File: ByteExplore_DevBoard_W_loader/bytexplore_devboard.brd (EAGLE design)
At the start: 68.6 x 53.3 mm, 87 parts, among them IC1 LM1117MPX-3.3, IC2 STM32F107RCT, IC4 MIC5219, IC6 STM32F103C8T, IC8 CP2101, J1 POWER_JACKPTH, Y1 SMD-CRYSTAL-8MHZ-20PF-20PPM(2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

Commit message: initial commit
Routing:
- net VDDA_PIN: track 47.5 -> 52.8 mm
- net GND: track 133.6 -> 137.7 mm, vias 53 -> 58
- added copper zone on layer 1, net N$49

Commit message: initial commit
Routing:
- net T_JTCK: track 58.0 -> 58.5 mm
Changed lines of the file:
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@@
 <drawing>
 <settings>
-<setting alwaysvectorfont="yes"/>
+<setting alwaysvectorfont="no"/>
 <setting verticaltext="up"/>
 </settings>
@@
 <wire x1="18.51" y1="22.86" x2="18.51" y2="22.98" width="0.25" layer="1"/>
 <via x="18.51" y="22.98" extent="1-16" drill="0.55"/>
-<wire x1="21.99" y1="24.57" x2="20.4" y2="22.98" width="0.25" layer="16"/>
-<wire x1="20.4" y1="22.98" x2="18.51" y2="22.98" width="0.25" layer="16"/>
-<wire x1="21.99" y1="24.57" x2="21.99" y2="26.55" width="0.25" layer="16"/>
-<wire x1="20.52" y1="28.02" x2="21.99" y2="26.55" width="0.254" layer="16"/>
+<wire x1="21.99" y1="23.7" x2="21.27" y2="22.98" width="0.25" layer="16"/>
+<wire x1="21.27" y1="22.98" x2="18.51" y2="22.98" width="0.25" layer="16"/>
+<wire x1="21.99" y1="23.7" x2="21.99" y2="27.15" width="0.25" layer="16"/>
+<wire x1="20.52" y1="28.62" x2="21.99" y2="27.15" width="0.254" layer="16"/>
 <via x="20.82" y="39.15" extent="1-16" drill="0.55"/>
 <wire x1="24.98" y1="39.53" x2="24.15" y2="38.7" width="0.254" layer="1"/>
@@
 <wire x1="25.44" y1="33.93" x2="22.32" y2="30.81" width="0.254" layer="16"/>
 <wire x1="21.33" y1="30.81" x2="20.52" y2="30" width="0.254" layer="16"/>
-<wire x1="20.52" y1="30" x2="20.52" y2="28.02" width="0.254" layer="16"/>
+<wire x1="20.52" y1="30" x2="20.52" y2="28.62" width="0.254" layer="16"/>
 <wire x1="11.955" y1="45.615" x2="11.955" y2="41.475" width="0.254" layer="16"/>
 <wire x1="11.955" y1="41.475" x2="13.5755375" y2="39.8544625" width="0.254" layer="16"/>

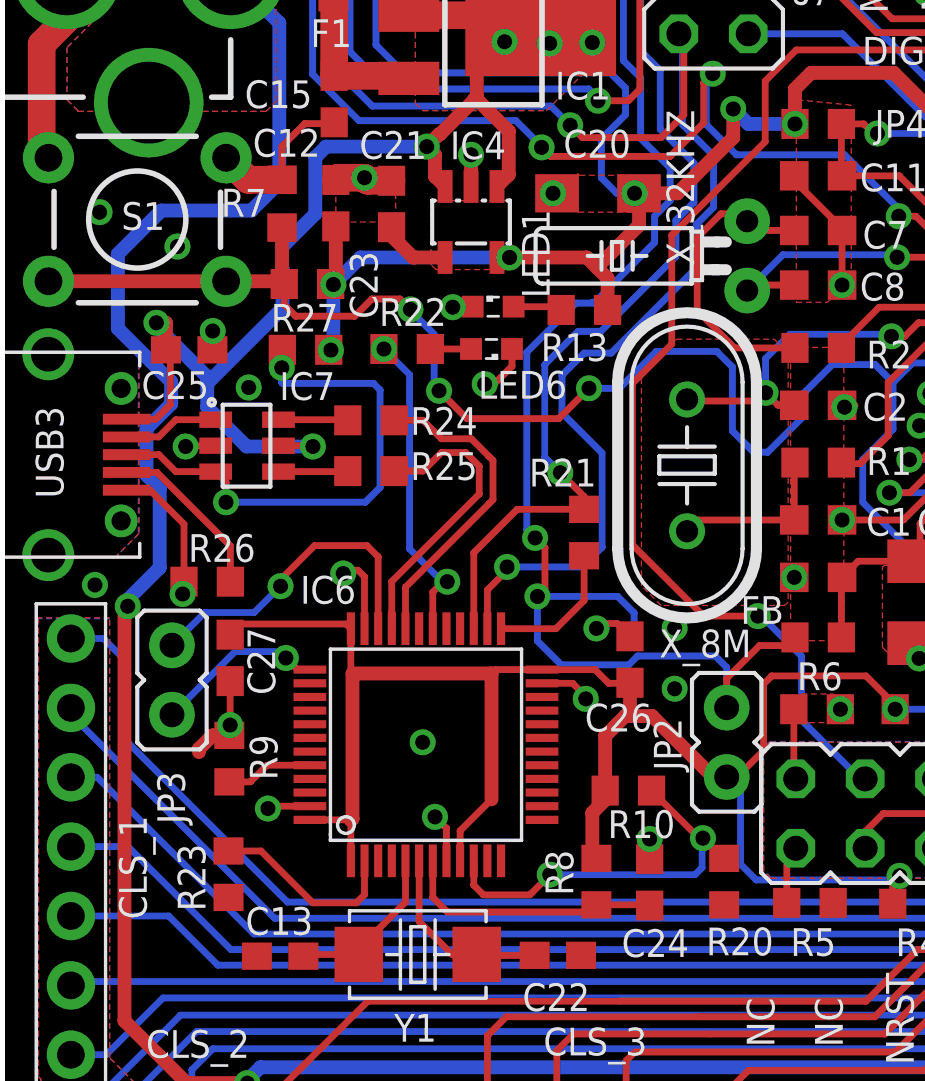
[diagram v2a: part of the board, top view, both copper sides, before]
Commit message: initial commit
change in power 3V wiring
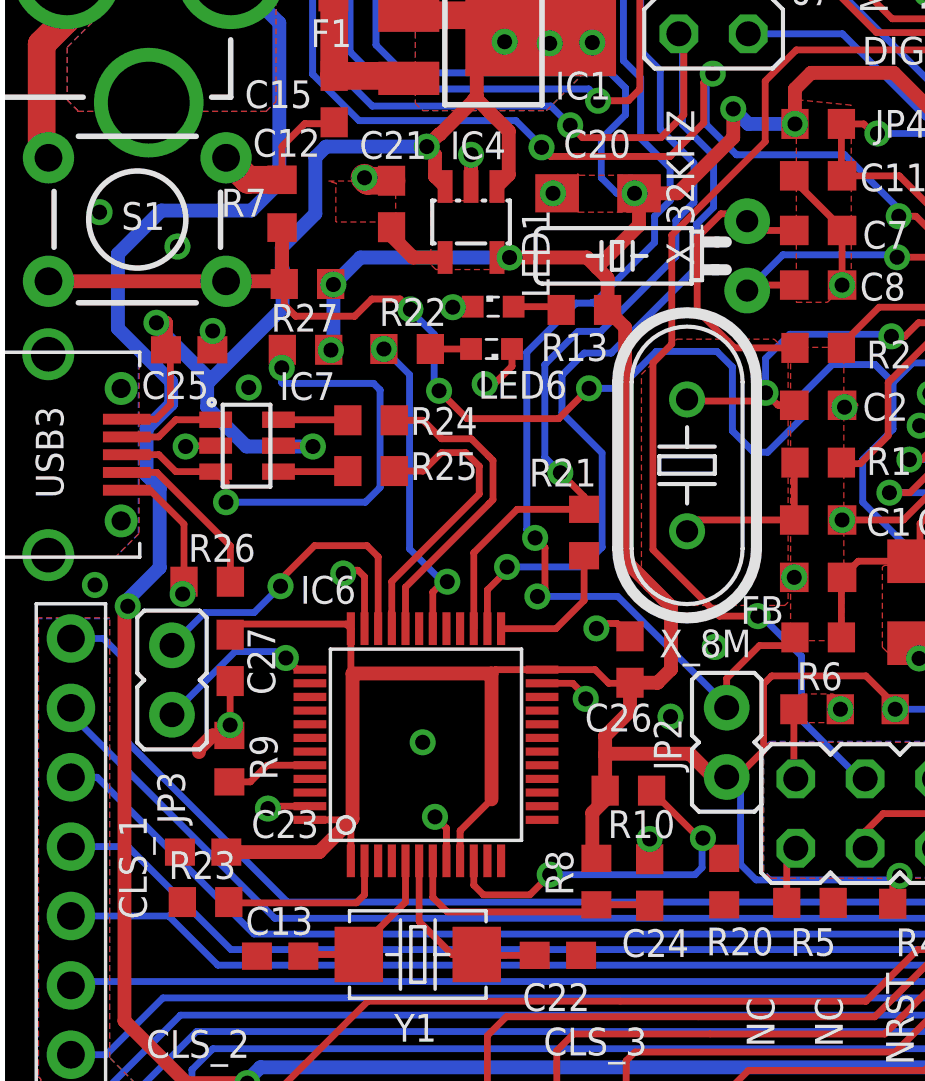
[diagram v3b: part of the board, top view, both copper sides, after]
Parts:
- moved C23 24.3 mm to (7.38, 12.5), turned to 0 degrees
- moved R23 1.32 mm to (7.47, 10.7), turned to 180 degrees
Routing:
- net +3V3: track 229.5 -> 248.5 mm
- net VDDA_PIN: track 52.8 -> 46.6 mm
- net GND: track 137.7 -> 136.6 mm
- net BOOT0: track 54.4 -> 53.5 mm
- net N$15: track 7.13 -> 6.35 mm
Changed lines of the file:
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@@
 <attribute name="VALUE" x="21.005" y="10.665" size="1.27" layer="27" rot="R180"/>
 </element>
-<element name="C23" library="rcl" library_urn="urn:adsk.eagle:library:334" package="C0603" package3d_urn="urn:adsk.eagle:package:23616/2" value="100nf" x="12.24" y="36.3" smashed="yes" rot="R270">
-<attribute name="NAME" x="12.755" y="34.535" size="1.016" layer="25" font="vector" ratio="15" rot="R270"/>
-<attribute name="POPULARITY" value="73" x="12.24" y="36.3" size="1.778" layer="27" rot="R270" display="off"/>
-<attribute name="SPICEPREFIX" value="C" x="12.24" y="36.3" size="1.778" layer="27" rot="R270" display="off"/>
-<attribute name="VALUE" x="10.335" y="36.935" size="1.27" layer="27" rot="R270"/>
+<element name="C23" library="rcl" library_urn="urn:adsk.eagle:library:334" package="C0603" package3d_urn="urn:adsk.eagle:package:23616/2" value="100nf" x="7.38" y="12.54" smashed="yes">
+<attribute name="NAME" x="9.145" y="13.055" size="1.016" layer="25" font="vector" ratio="15"/>
+<attribute name="POPULARITY" value="73" x="7.38" y="12.54" size="1.778" layer="27" display="off"/>
+<attribute name="SPICEPREFIX" value="C" x="7.38" y="12.54" size="1.778" layer="27" display="off"/>
+<attribute name="VALUE" x="6.745" y="10.635" size="1.27" layer="27"/>
 </element>
 <element name="C24" library="rcl" library_urn="urn:adsk.eagle:library:334" package="C0603" package3d_urn="urn:adsk.eagle:package:23616/2" value="100nf" x="23.73" y="11.43" smashed="yes" rot="R270">
@@
 <attribute name="VALUE" x="18.94" y="32.96" size="1.27" layer="27" rot="R180"/>
 </element>
-<element name="R23" library="rcl" library_urn="urn:adsk.eagle:library:334" package="R0603" package3d_urn="urn:adsk.eagle:package:23555/3" value="10k" x="8.31" y="11.73" smashed="yes" rot="R270">
-<attribute name="NAME" x="7.465" y="10.375" size="1.016" layer="25" font="vector" ratio="15" rot="R90"/>
-<attribute name="POPULARITY" value="77" x="8.31" y="11.73" size="1.778" layer="27" rot="R270" display="off"/>
-<attribute name="SPICEPREFIX" value="R" x="8.31" y="11.73" size="1.778" layer="27" rot="R270" display="off"/>
-<attribute name="VALUE" x="6.405" y="12.365" size="1.27" layer="27" rot="R270"/>
+<element name="R23" library="rcl" library_urn="urn:adsk.eagle:library:334" package="R0603" package3d_urn="urn:adsk.eagle:package:23555/3" value="10k" x="7.47" y="10.71" smashed="yes" rot="R180">
+<attribute name="NAME" x="6.115" y="11.555" size="1.016" layer="25" font="vector" ratio="15"/>
+<attribute name="POPULARITY" value="77" x="7.47" y="10.71" size="1.778" layer="27" rot="R180" display="off"/>
+<attribute name="SPICEPREFIX" value="R" x="7.47" y="10.71" size="1.778" layer="27" rot="R180" display="off"/>
+<attribute name="VALUE" x="8.105" y="12.615" size="1.27" layer="27" rot="R180"/>
 </element>
 <element name="C25" library="rcl" library_urn="urn:adsk.eagle:library:334" package="C0603" package3d_urn="urn:adsk.eagle:package:23616/2" value="" x="6.87" y="30.93" smashed="yes" rot="R180">
@@
 <wire x1="16.29" y1="12.22" x2="16.29" y2="13.41" width="0.254" layer="1"/>
 <wire x1="16.29" y1="13.41" x2="15.87" y2="13.83" width="0.254" layer="1"/>
-<via x="24.645" y="20.74" extent="1-16" drill="0.55"/>
+<via x="26.115" y="20.05" extent="1-16" drill="0.55"/>
 <via x="36" y="36.3" extent="1-16" drill="0.55"/>
 <wire x1="37.43" y1="27.62" x2="38.29" y2="27.62" width="0.254" layer="1"/>
@@
 <via x="16.14" y="1.05" extent="1-16" drill="0.55"/>
 <via x="48.12" y="4.5" extent="1-16" drill="0.55"/>
-<wire x1="12.24" y1="37.15" x2="12.32" y2="37.23" width="1.016" layer="1"/>
-<wire x1="12.32" y1="37.23" x2="13.29" y2="37.23" width="1.016" layer="1"/>
 <wire x1="14.28" y1="37.12" x2="13.4" y2="37.12" width="1.016" layer="1"/>
 <wire x1="13.4" y1="37.12" x2="13.29" y2="37.23" width="1.016" layer="1"/>
@@
 <wire x1="63.97149375" y1="36.467" x2="64.962246875" y2="37.457753125" width="0.508" layer="1"/>
 <wire x1="11.7" y1="1.08" x2="11.7" y2="2.91" width="0.508" layer="16"/>
-<via x="24.645" y="18.52" extent="1-16" drill="0.55"/>
+<via x="24.495" y="17.5" extent="1-16" drill="0.55"/>
 <via x="63.63" y="5.73" extent="1-16" drill="0.55"/>
 <via x="63.96" y="11.01" extent="1-16" drill="0.55"/>
@@
 <wire x1="27.96" y1="40.77" x2="27.96" y2="38.55" width="0.25" layer="1"/>
 <wire x1="27.96" y1="38.55" x2="24.54" y2="35.13" width="0.25" layer="1"/>
-<wire x1="24.54" y1="31.14" x2="23.1" y2="29.7" width="0.25" layer="1"/>
-<wire x1="23.1" y1="29.7" x2="23.1" y2="23.79" width="0.25" layer="1"/>
-<wire x1="25.71" y1="21.18" x2="27.69" y2="21.18" width="0.25" layer="1"/>
+<wire x1="24.54" y1="31.14" x2="23.85" y2="30.45" width="0.25" layer="1"/>
+<wire x1="23.85" y1="30.45" x2="23.85" y2="23.61" width="0.25" layer="1"/>
+<wire x1="26.28" y1="21.18" x2="27.69" y2="21.18" width="0.25" layer="1"/>
 <via x="27.69" y="21.18" extent="1-16" drill="0.55"/>
 <wire x1="27.69" y1="21.18" x2="27.82" y2="21.18" width="0.25" layer="16"/>
 <wire x1="29.29" y1="19.71" x2="27.82" y2="21.18" width="0.25" layer="16"/>
 <wire x1="24.54" y1="35.13" x2="24.54" y2="31.14" width="0.25" layer="1"/>
-<wire x1="23.1" y1="23.79" x2="25.71" y2="21.18" width="0.25" layer="1"/>
+<wire x1="23.85" y1="23.61" x2="26.28" y2="21.18" width="0.25" layer="1"/>
 <wire x1="29.29" y1="17.37" x2="29.29" y2="19.71" width="0.25" layer="16"/>
 <contactref element="JP1" pad="4"/>
@@
 <wire x1="12.79" y1="19.14" x2="12.85" y2="19.08" width="0.25" layer="1"/>
 <wire x1="23.01" y1="18.74" x2="23.01" y2="17.7" width="0.508" layer="1"/>
-<wire x1="22.1" y1="16.79" x2="22.1" y2="14.79" width="0.508" layer="1"/>
-<wire x1="23.01" y1="17.7" x2="22.83" y2="17.52" width="0.508" layer="1"/>
-<wire x1="22.83" y1="17.52" x2="22.1" y2="16.79" width="0.508" layer="1"/>
+<wire x1="22.1" y1="16.79" x2="22.1" y2="16.11" width="0.508" layer="1"/>
+<wire x1="22.1" y1="16.11" x2="22.1" y2="14.79" width="0.508" layer="1"/>
+<wire x1="23.01" y1="17.7" x2="22.1" y2="16.79" width="0.508" layer="1"/>
 <wire x1="22.1" y1="14.79" x2="22.1" y2="14.45" width="0.508" layer="1"/>
 <wire x1="22.1" y1="14.45" x2="21.63" y2="13.98" width="0.508" layer="1"/>
@@
 <wire x1="12.05" y1="33.34" x2="12.07" y2="33.32" width="0.508" layer="1"/>
 <wire x1="12.15" y1="33.32" x2="12.07" y2="33.32" width="0.508" layer="1"/>
-<wire x1="12.24" y1="35.45" x2="12.24" y2="33.41" width="0.508" layer="1"/>
 <wire x1="12.24" y1="33.41" x2="12.15" y2="33.32" width="0.508" layer="1"/>
 <wire x1="11.55" y1="50.86" x2="13.71" y2="48.7" width="0.254" layer="16"/>
@@
 <wire x1="16.79" y1="13.32" x2="17.94" y2="14.47" width="0.254" layer="1"/>
 <wire x1="26.55" y1="15.29" x2="26.05" y2="15.29" width="0.508" layer="1"/>
-<wire x1="23.82" y1="17.52" x2="22.83" y2="17.52" width="0.508" layer="1"/>
-<wire x1="26.05" y1="15.29" x2="23.82" y2="17.52" width="0.508" layer="1"/>
+<wire x1="26.05" y1="15.29" x2="25.2" y2="16.14" width="0.508" layer="1"/>
 <wire x1="12.79" y1="13.7" x2="12.79" y2="13.71" width="0.254" layer="1"/>
 <wire x1="12.79" y1="13.71" x2="12.8" y2="13.72" width="0.254" layer="1"/>
+<wire x1="8.23" y1="12.54" x2="11.63" y2="12.54" width="0.508" layer="1"/>
+<wire x1="11.63" y1="12.54" x2="12.79" y2="13.7" width="0.508" layer="1"/>
+<wire x1="25.2" y1="16.14" x2="22.13" y2="16.14" width="0.508" layer="1"/>
+<wire x1="22.13" y1="16.14" x2="22.1" y2="16.11" width="0.508" layer="1"/>
+<wire x1="22.19" y1="32.39" x2="22.83" y2="31.75" width="0.508" layer="1"/>
+<wire x1="24.51" y1="21.54" x2="24.51" y2="19.23" width="0.508" layer="1"/>
+<wire x1="24.51" y1="19.23" x2="24.02" y2="18.74" width="0.508" layer="1"/>
+<wire x1="24.02" y1="18.74" x2="23.01" y2="18.74" width="0.508" layer="1"/>
+<wire x1="22.83" y1="31.75" x2="22.83" y2="23.22" width="0.508" layer="1"/>
+<wire x1="22.83" y1="23.22" x2="24.51" y2="21.54" width="0.508" layer="1"/>
 </signal>
 <signal name="VBAT">
@@
 <wire x1="19.5365875" y1="24.0432" x2="19.8965875" y2="23.6832" width="0.254" layer="1"/>
 <via x="19.62" y="21.9" extent="1-16" drill="0.55"/>
-<wire x1="26.55" y1="19.3" x2="26.55" y2="17.83" width="0.254" layer="16"/>
-<wire x1="26.55" y1="19.3" x2="26.13" y2="19.72" width="0.254" layer="16"/>
 <wire x1="19.23" y1="24.3497875" x2="19.5365875" y2="24.0432" width="0.254" layer="16"/>
 <wire x1="19.23" y1="30.84" x2="19.23" y2="24.3497875" width="0.254" layer="16"/>
 <wire x1="22.77" y1="41.52" x2="23.4" y2="40.89" width="0.254" layer="16"/>
-<wire x1="23.29" y1="19.72" x2="26.13" y2="19.72" width="0.254" layer="16"/>
-<wire x1="22.965" y1="19.395" x2="23.29" y2="19.72" width="0.254" layer="16"/>
-<wire x1="20.4955625" y1="19.395" x2="19.62" y2="20.2705625" width="0.254" layer="16"/>
-<wire x1="19.62" y1="21.9" x2="19.62" y2="20.2705625" width="0.254" layer="16"/>
-<wire x1="20.4955625" y1="19.395" x2="22.965" y2="19.395" width="0.254" layer="16"/>
 <wire x1="19.62" y1="21.9" x2="22.56" y2="21.9" width="0.254" layer="16"/>
-<wire x1="22.56" y1="21.9" x2="23.16" y2="21.3" width="0.254" layer="16"/>
-<wire x1="23.16" y1="21.3" x2="23.16" y2="20.28" width="0.254" layer="16"/>
+<wire x1="22.56" y1="21.9" x2="26.725" y2="17.735" width="0.25" layer="16"/>
+<wire x1="26.55" y1="17.56" x2="26.55" y2="17.83" width="0.25" layer="16"/>
+<wire x1="26.55" y1="17.56" x2="26.725" y2="17.735" width="0.25" layer="16"/>
 </signal>
 <signal name="RX">
@@
 <contactref element="R23" pad="1"/>
 <wire x1="13.29" y1="12.22" x2="13.29" y2="10.98" width="0.25" layer="1"/>
-<wire x1="11.4" y1="10.68" x2="9.5" y2="12.58" width="0.25" layer="1"/>
-<wire x1="9.5" y1="12.58" x2="8.31" y2="12.58" width="0.25" layer="1"/>
 <wire x1="13.29" y1="10.98" x2="12.99" y2="10.68" width="0.25" layer="1"/>
-<wire x1="12.99" y1="10.68" x2="11.4" y2="10.68" width="0.25" layer="1"/>
+<wire x1="8.35" y1="10.68" x2="8.32" y2="10.71" width="0.25" layer="1"/>
+<wire x1="12.99" y1="10.68" x2="8.35" y2="10.68" width="0.25" layer="1"/>
 </signal>
 <signal name="F3SWDIO">
